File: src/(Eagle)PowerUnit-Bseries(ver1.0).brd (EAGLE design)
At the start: 100 x 100 mm, 84 parts, among them CON1 XT90PW-M, CON2 XT90PW-F, CON3 XT60PW-F, CON4 XT60PW-F, CON5 XT60PW-F, CON6 XT60PW-F, Q1 DMP3056L-7, Q3 DMP3056L-7, U1 LQFP64, U2 MCP2517FD, U3 CH340E, U4 AP63203WU-7, U5 AP63205WU-7, U6 AP331AWG-7, U8 AP331AWG-7

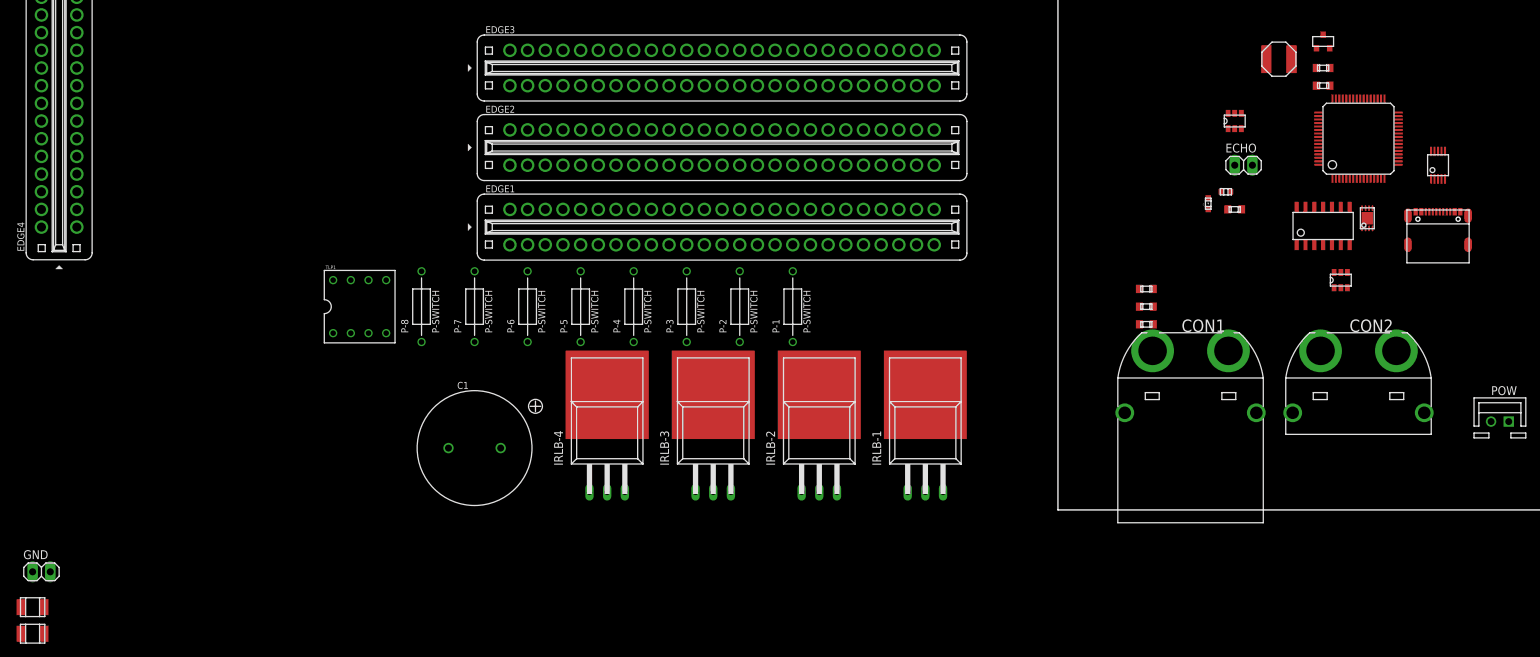
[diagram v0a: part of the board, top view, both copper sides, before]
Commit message: 5VDCDCの出力コンをOSコンにした
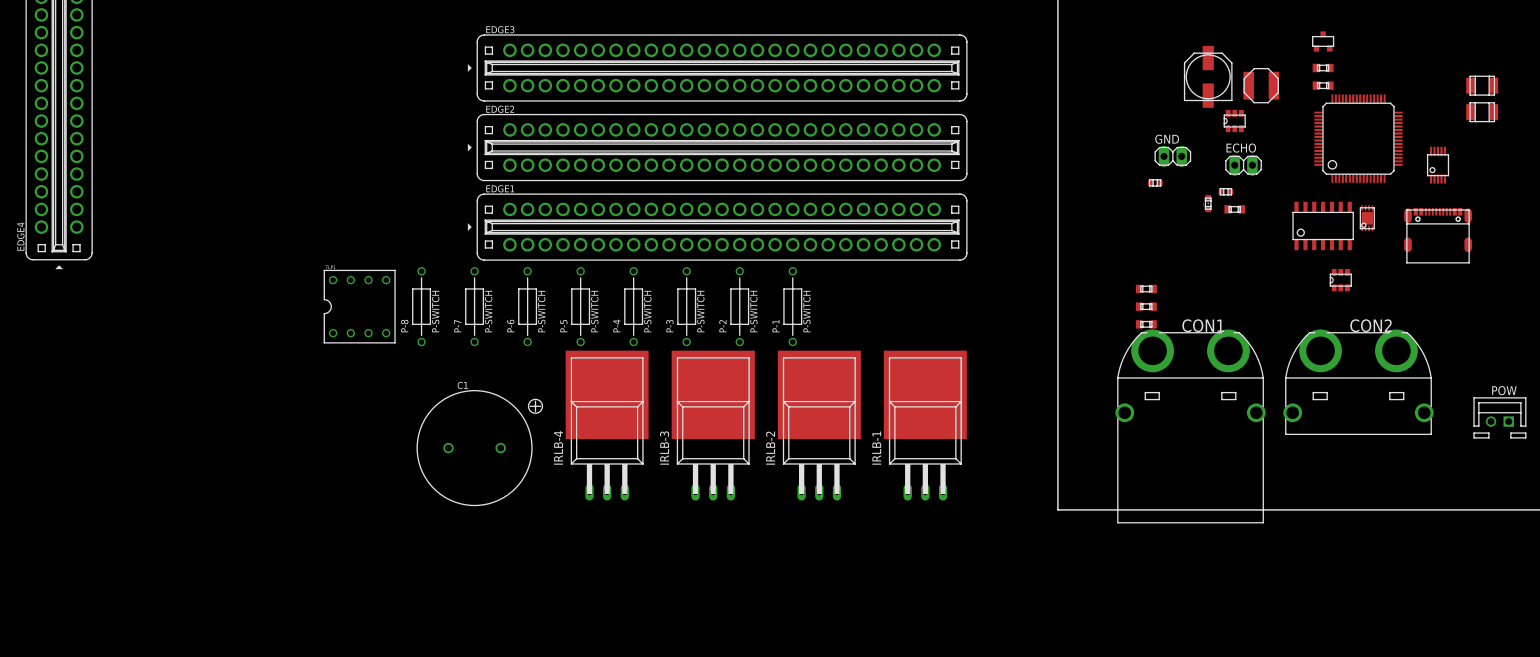
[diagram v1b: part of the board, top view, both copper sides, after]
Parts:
- added C6: GCM188L81H104KA57, GCM188L81H104K57(0.1uF):GCM188L81H104KA57
- added C7: A768EB566M1VLAE042, A768EB566M1VLAE042:A768EB566M1VLAE042
- moved C4 221.3 mm to (61.0, 61.0)
- moved C5 221.3 mm to (61.0, 57.1)
- moved GND 173.2 mm to (16.5, 50.8)
- moved L1 4.58 mm to (29.2, 61.0)
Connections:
- new net +5V: C7.ANODE, L1.R, U5.FB
- new net N$41: C6.P$1, U5.BST
- net GND2: now also C7.CATHODE
- net N$40: now also C6.P$2
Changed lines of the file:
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@@
 <attribute name="NAME" x="20.955" y="43.688" size="0.127" layer="25" rot="R90"/>
 </element>
-<element name="GND" library="pinhead" library_urn="urn:adsk.eagle:library:325" package="1X02" package3d_urn="urn:adsk.eagle:package:22435/2" value="" x="-146.05" y="-8.89" smashed="yes">
-<attribute name="NAME" x="-148.6662" y="-7.0612" size="1.27" layer="25" ratio="10"/>
-<attribute name="POPULARITY" value="98" x="-146.05" y="-8.89" size="1.778" layer="27" display="off"/>
-<attribute name="VALUE" x="-148.59" y="-12.065" size="1.27" layer="27"/>
+<element name="GND" library="pinhead" library_urn="urn:adsk.eagle:library:325" package="1X02" package3d_urn="urn:adsk.eagle:package:22435/2" value="" x="16.51" y="50.8" smashed="yes">
+<attribute name="NAME" x="13.8938" y="52.6288" size="1.27" layer="25" ratio="10"/>
+<attribute name="POPULARITY" value="98" x="16.51" y="50.8" size="1.778" layer="27" display="off"/>
+<attribute name="VALUE" x="13.97" y="47.625" size="1.27" layer="27"/>
 </element>
 <element name="Q1" library="DMP3056L-7" package="SOT23" value="DMP3056L-7" x="38.1" y="67.31" smashed="yes">
@@
 <attribute name="VALUE" x="36.8" y="61.66" size="0.5" layer="27"/>
 </element>
-<element name="L1" library="NRS5030T4R7MMGJ" package="NRS5030T4R7MMGJ" value="4.7uH" x="31.75" y="64.77" smashed="yes">
-<attribute name="VALUE" x="30.607" y="61.468" size="0.5" layer="27"/>
-</element>
-<element name="C4" library="GRM32ER71H106KA12" package="GRM32ER71H106KA12" value="GRM32ER71H106KA12" x="-147.32" y="-13.97" smashed="yes">
-<attribute name="VALUE" x="-148.72" y="-12.47" size="0.5" layer="27"/>
-</element>
-<element name="C5" library="GRM32ER71H106KA12" package="GRM32ER71H106KA12" value="GRM32ER71H106KA12" x="-147.32" y="-17.78" smashed="yes">
-<attribute name="VALUE" x="-148.72" y="-16.28" size="0.5" layer="27"/>
+<element name="L1" library="NRS5030T4R7MMGJ" package="NRS5030T4R7MMGJ" value="4.7uH" x="29.21" y="60.96" smashed="yes">
+<attribute name="VALUE" x="28.067" y="57.658" size="0.5" layer="27"/>
+</element>
+<element name="C4" library="GRM32ER71H106KA12" package="GRM32ER71H106KA12" value="GRM32ER71H106KA12" x="60.96" y="60.96" smashed="yes">
+<attribute name="VALUE" x="59.56" y="62.46" size="0.5" layer="27"/>
+</element>
+<element name="C5" library="GRM32ER71H106KA12" package="GRM32ER71H106KA12" value="GRM32ER71H106KA12" x="60.96" y="57.15" smashed="yes">
+<attribute name="VALUE" x="59.56" y="58.65" size="0.5" layer="27"/>
+</element>
+<element name="C6" library="GCM188L81H104K57(0.1uF)" package="GCM188L81H104KA57" value="GCM188L81H104KA57" x="13.97" y="46.99" smashed="yes">
+<attribute name="NAME" x="13.17" y="47.49" size="0.1" layer="21"/>
+</element>
+<element name="C7" library="A768EB566M1VLAE042" package="A768EB566M1VLAE042" value="A768EB566M1VLAE042" x="21.59" y="62.23" smashed="yes" rot="R90">
+<attribute name="VALUE" x="17.78" y="59.69" size="1" layer="27" rot="R90"/>
 </element>
 </elements>
@@
 <contactref element="U2" pad="VSS"/>
 <contactref element="GND" pad="2"/>
-<wire x1="-87.57" y1="8.89" x2="-144.78" y2="-8.89" width="0" layer="19" extent="1-1"/>
+<wire x1="-87.57" y1="8.89" x2="17.78" y2="50.8" width="0" layer="19" extent="1-1"/>
 <wire x1="-96.52" y1="33.02" x2="-87.57" y2="8.89" width="0" layer="19" extent="1-1"/>
 <wire x1="-62.23" y1="2.54" x2="-87.57" y2="8.89" width="0" layer="19" extent="1-1"/>
@@
 <contactref element="C5" pad="R"/>
 <contactref element="C4" pad="R"/>
-<wire x1="-145.62" y1="-13.97" x2="-145.62" y2="-17.78" width="0" layer="19" extent="1-1"/>
-<wire x1="-147.32" y1="-8.89" x2="-145.62" y2="-13.97" width="0" layer="19" extent="1-1"/>
-<wire x1="-140.97" y1="99.06" x2="-147.32" y2="-8.89" width="0" layer="19" extent="1-1"/>
+<contactref element="C7" pad="CATHODE"/>
+<wire x1="15.24" y1="50.8" x2="21.59" y2="59.53" width="0" layer="19" extent="1-1"/>
+<wire x1="-140.97" y1="99.06" x2="15.24" y2="50.8" width="0" layer="19" extent="1-1"/>
 <wire x1="-33.02" y1="105.41" x2="-140.97" y2="99.06" width="0" layer="19" extent="1-1"/>
 <wire x1="-20.32" y1="60.96" x2="-33.02" y2="105.41" width="0" layer="19" extent="1-1"/>
@@
 <wire x1="58.93" y1="42.28" x2="57.81" y2="42.84" width="0" layer="19" extent="1-1"/>
 <wire x1="58.93" y1="38.1" x2="58.93" y2="42.28" width="0" layer="19" extent="1-1"/>
-<wire x1="71.39" y1="46.99" x2="58.93" y2="42.28" width="0" layer="19" extent="1-1"/>
-<wire x1="71.39" y1="52.07" x2="71.39" y2="46.99" width="0" layer="19" extent="1-1"/>
-<wire x1="72.39" y1="57.07" x2="71.39" y2="52.07" width="0" layer="19" extent="1-1"/>
+<wire x1="62.66" y1="57.15" x2="54.61" y2="47.555" width="0" layer="19" extent="1-1"/>
+<wire x1="62.66" y1="60.96" x2="62.66" y2="57.15" width="0" layer="19" extent="1-1"/>
+<wire x1="72.39" y1="57.07" x2="62.66" y2="57.15" width="0" layer="19" extent="1-1"/>
+<wire x1="71.39" y1="52.07" x2="72.39" y2="57.07" width="0" layer="19" extent="1-1"/>
+<wire x1="71.39" y1="46.99" x2="71.39" y2="52.07" width="0" layer="19" extent="1-1"/>
 <wire x1="72.39" y1="18.97" x2="58.93" y2="38.1" width="0" layer="19" extent="1-1"/>
 <wire x1="71.39" y1="11.43" x2="72.39" y2="18.97" width="0" layer="19" extent="1-1"/>
@@
 <contactref element="C4" pad="L"/>
 <contactref element="C5" pad="L"/>
-<wire x1="-149.02" y1="-13.97" x2="-149.02" y2="-17.78" width="0" layer="19" extent="1-1"/>
-<wire x1="26.35" y1="54.7805" x2="-149.02" y2="-13.97" width="0" layer="19" extent="1-1"/>
+<wire x1="59.26" y1="60.96" x2="59.26" y2="57.15" width="0" layer="19" extent="1-1"/>
+<wire x1="26.35" y1="54.7805" x2="59.26" y2="60.96" width="0" layer="19" extent="1-1"/>
 <wire x1="39.1" y1="63.5" x2="26.35" y2="54.7805" width="0" layer="19" extent="1-1"/>
 <wire x1="39.05" y1="66.31" x2="39.1" y2="63.5" width="0" layer="19" extent="1-1"/>
@@
 <contactref element="L1" pad="L"/>
 <contactref element="U5" pad="SW"/>
-<wire x1="25.4" y1="56.9795" x2="29.95" y2="64.77" width="0" layer="19" extent="1-1"/>
+<contactref element="C6" pad="P$2"/>
+<wire x1="25.4" y1="56.9795" x2="14.67" y2="46.99" width="0" layer="19" extent="1-1"/>
+<wire x1="27.41" y1="60.96" x2="25.4" y2="56.9795" width="0" layer="19" extent="1-1"/>
+</signal>
+<signal name="N$41">
+<contactref element="C6" pad="P$1"/>
+<contactref element="U5" pad="BST"/>
+<wire x1="24.45" y1="56.9795" x2="13.27" y2="46.99" width="0" layer="19" extent="1-1"/>
+</signal>
+<signal name="+5V">
+<contactref element="C7" pad="ANODE"/>
+<contactref element="L1" pad="R"/>
+<contactref element="U5" pad="FB"/>
+<wire x1="24.45" y1="54.7805" x2="21.59" y2="64.93" width="0" layer="19" extent="1-1"/>
+<wire x1="31.01" y1="60.96" x2="24.45" y2="54.7805" width="0" layer="19" extent="1-1"/>
 </signal>
 </signals>

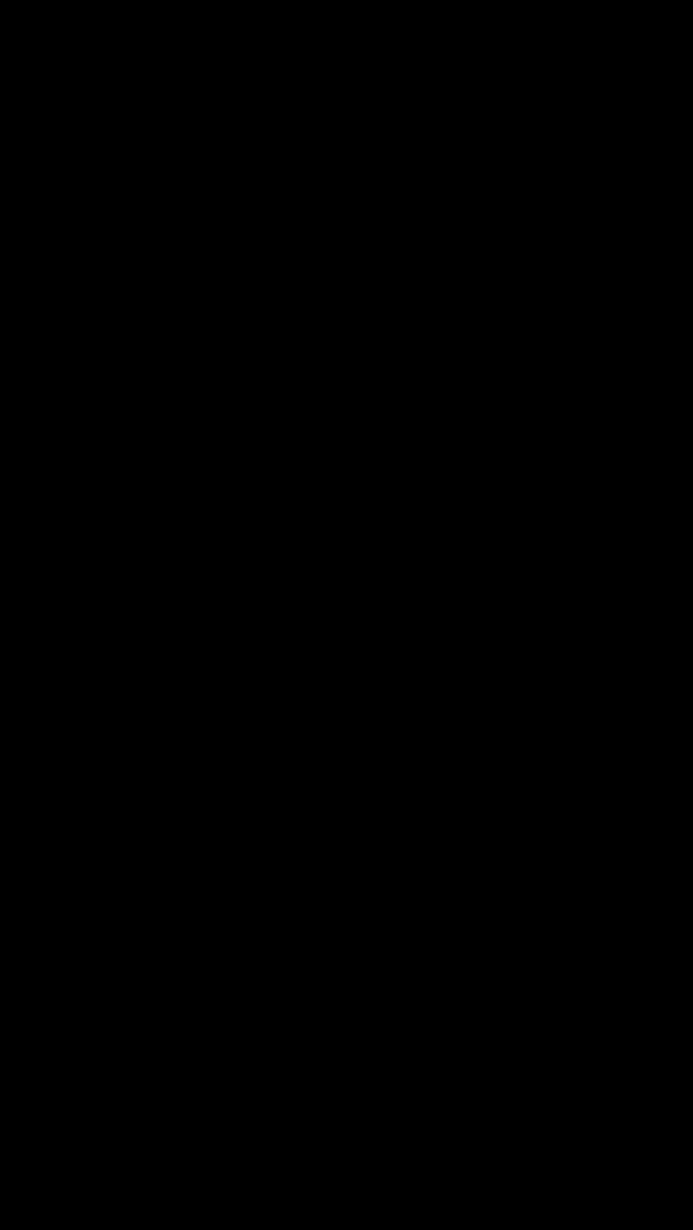
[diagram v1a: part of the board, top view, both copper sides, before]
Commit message: +5V周りの冗長性を高める回路を構成(大晦日ですよ？（笑）)
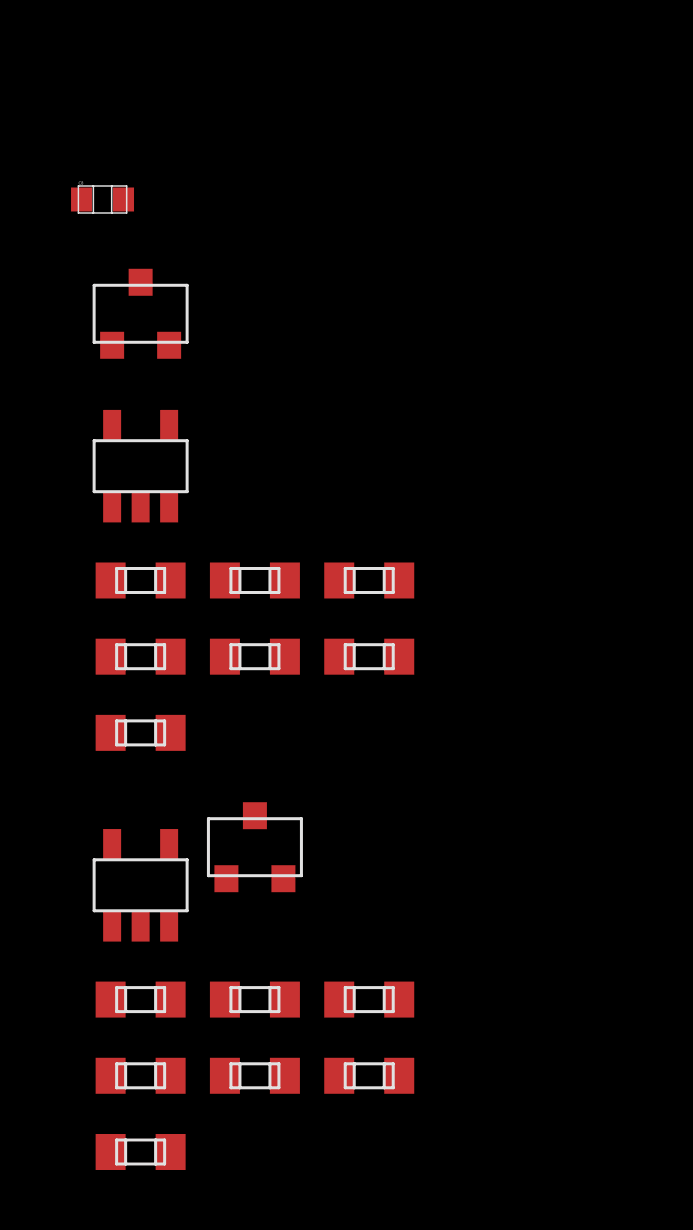
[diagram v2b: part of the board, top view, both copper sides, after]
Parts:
- added C8: GCM188L81H104KA57, GCM188L81H104K57(0.1uF):GCM188L81H104KA57
- added Q2, Q4: SSM3J332R, SSM3J332R:SOT-23F
- added R20, R21, R22, R23, R24, R34, R35, R36, R37, R38: 10k, CR0603:CR0603
- added R32, R39: 100k, CR0603:CR0603
- added R33, R40: 0, CR0603:CR0603
- added U7, U9: AP331AWG-7, AP331AWG-7:SOT25
- R18: value 0 -> 12k
- R19: value ∞ -> 3k
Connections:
- new net N$43: Q2.G, R20.RIGHT, R32.LEFT, R33.LEFT, R33.RIGHT, U7.OUTPUT
- new net N$44: R21.LEFT, R22.RIGHT, U7.IN-
- new net N$47: R23.LEFT, R24.RIGHT, U7.IN+
- new net N$51: Q4.G, R34.RIGHT, R39.LEFT, R40.LEFT, R40.RIGHT, U9.OUTPUT
- new net N$52: R35.LEFT, R36.RIGHT, U9.IN-
- new net N$53: R37.LEFT, R38.RIGHT, U9.IN+
- new net N$55: C7.ANODE, L1.R, Q2.D, R21.RIGHT, U5.FB
- net +5V: now also Q2.S, Q4.S, R20.LEFT, R23.RIGHT, R32.RIGHT, R34.LEFT, R37.RIGHT, R39.RIGHT, U7.VCC, U9.VCC; no longer C7.ANODE, L1.R, U5.FB
- net GND2: now also C8.P$2, R22.LEFT, R24.LEFT, R36.LEFT, R38.LEFT, U7.GND, U9.GND
- net U5V: now also Q4.D, R35.RIGHT
- net V+: now also C8.P$1

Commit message: CANコントローラのXtal選定
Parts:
- removed JP2: (no value), pinhead:1X02
- removed Q1, Q3: DMP3056L-7, DMP3056L-7:SOT23
- removed R11, R12, R13, R14, R15, R25, R26, R27, R28, R29: 10k, CR0603:CR0603
- removed R16, R30: 100k, CR0603:CR0603
- removed R17, R31: 0, CR0603:CR0603
- removed U4: AP63203WU-7, AP63203WU-7:AP63203WU-7
- removed U6, U8: AP331AWG-7, AP331AWG-7:SOT25
- added C10, C11, C13: GCM188L81H104KA57, GCM188L81H104K57(0.1uF):GCM188L81H104KA57
- added C12, C9: GRM32ER71E226KE15, GRM32ER71E226KE15:3225M
- added D1, D2: GS1010FL, GS1010FL:GS1010FL
- added SW1: SS-12SDP2, SS-12SDP2:SS-12SDP2
- added U$4: AZ1117CH-3.3TRG1, AZ1117CH-3.3TRG1:AZ1117C
- added X1: XRCGB40M000F4M00R0, XRCGB40M000F4M00R0:XRCGB40M000F4M00R0
- moved C8 223.3 mm to (63.5, 63.5)
- moved Q2 223.3 mm to (64.8, 59.7)
- moved Q4 223.3 mm to (68.6, 41.9)
- moved R20 223.3 mm to (64.8, 50.8)
- moved R21 223.3 mm to (68.6, 50.8)
- moved R22 223.3 mm to (72.4, 50.8)
- moved R23 223.3 mm to (64.8, 48.3)
- moved R24 223.3 mm to (68.6, 48.3)
- moved R32 223.3 mm to (72.4, 48.3)
- moved R33 223.3 mm to (64.8, 45.7)
- moved R34 223.3 mm to (64.8, 36.8)
- moved R35 223.3 mm to (68.6, 36.8)
- moved R36 223.3 mm to (72.4, 36.8)
- moved R37 223.3 mm to (64.8, 34.3)
- moved R38 223.3 mm to (68.6, 34.3)
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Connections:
- removed net N$38 (its old number): R12.LEFT, R13.RIGHT, U6.IN-
- removed net N$45: POW.2, Q3.D, R26.RIGHT
- removed net N$46: Q3.G, R25.RIGHT, R30.LEFT, R31.LEFT, R31.RIGHT, U8.OUTPUT
- removed net N$48: R26.LEFT, R27.RIGHT, U8.IN-
- removed net N$49: R28.LEFT, R29.RIGHT, U8.IN+
- new net CS: U1.P33, U2.NCS
- new net MISO: U1.P35, U2.SDO
- new net MOSI: U1.P36, U2.SDI
- new net N$42: U2.OSC2, X1.1
- new net SCK: U1.P34, U2.SCK
- net +3V3: now also C11.P$1, C12.L, C13.P$2, U$1.VIO, U$4.OUTPUT, U$4.VOUT, U2.VDD
- net +5V: now also C10.P$1, C9.L, U$1.VDD, U$4.INPUT
- net CANL: now also SW1.C; no longer JP2.2
- net GND: no longer U$1.EP, U$1.VSS, U2.VSS
- net GND2: now also C10.P$2, C11.P$2, C12.R, C13.P$1, C9.R, U$1.EP, U$1.VSS, U$4.GND, U2.VSS; no longer R13.LEFT, R15.LEFT, R27.LEFT, R29.LEFT, U4.GND, U6.GND, U8.GND
- net N$23: now also SW1.R; no longer JP2.1
- net N$35: now also D1.A; no longer Q1.D, R12.RIGHT
- net N$37: now also D2.A, POW.2; no longer Q1.G, R11.RIGHT, R16.LEFT, R17.LEFT, R17.RIGHT, U6.OUTPUT
- net N$39: now also U2.OSC1, X1.2; no longer R14.LEFT, R15.RIGHT, U6.IN+
- net V+: now also D1.C, D2.C; no longer Q1.S, Q3.S, R11.LEFT, R14.RIGHT, R16.RIGHT, R25.LEFT, R28.RIGHT, R30.RIGHT, U6.VCC, U8.VCC
